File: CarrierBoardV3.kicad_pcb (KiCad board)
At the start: 4 copper layers, 92 x 96 mm, 102 parts, among them J1 USB_B_Micro, J10 Conn_02x26_Odd_Even, J11 SW1-12V_SHUNT, J12 SW9-3V3_SHUNT, J13 SW5-5V_SHUNT, J2 Conn_02x09_Odd_Even, J3 Barrel_Jack, J4 TX2iConnctor, J5 Conn_01x03_Male, J6 Conn_02x04_Odd_Even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

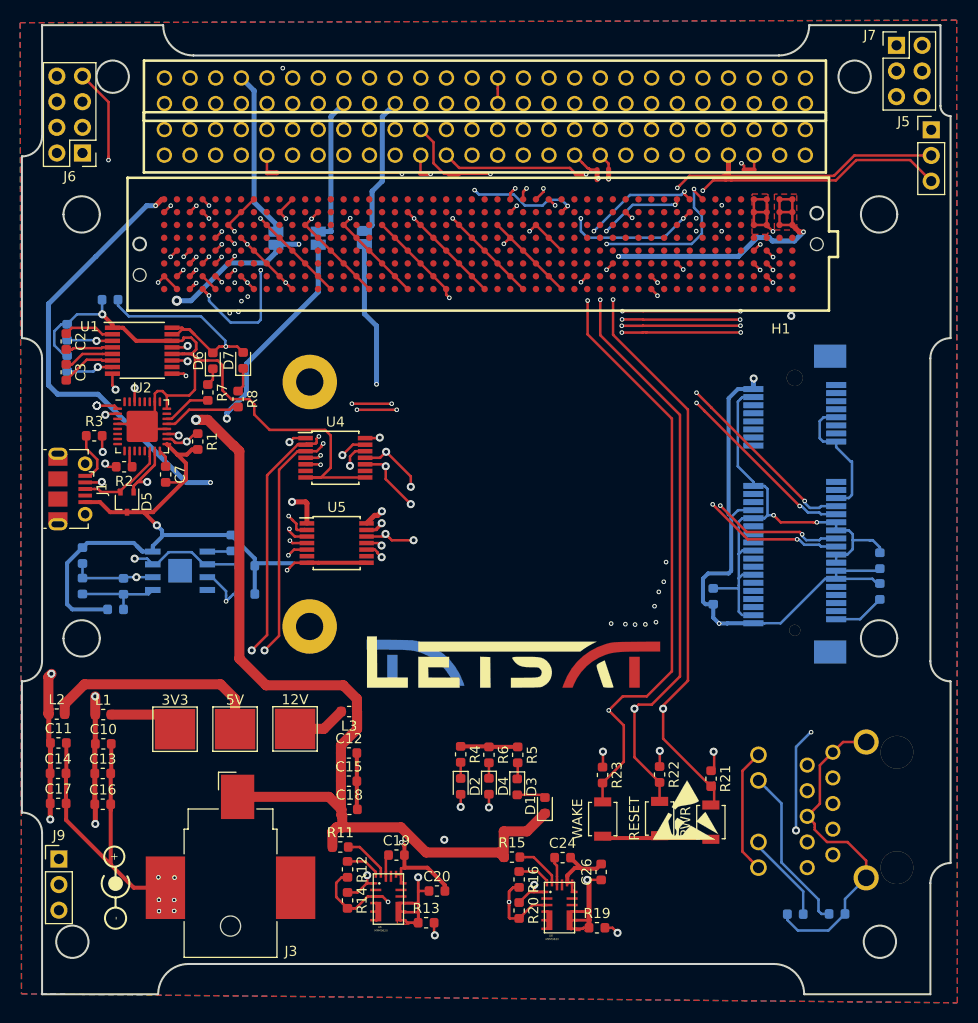
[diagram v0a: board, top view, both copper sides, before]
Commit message: traces complete, need help length matching becasue I can not seem to get it, no idea why???
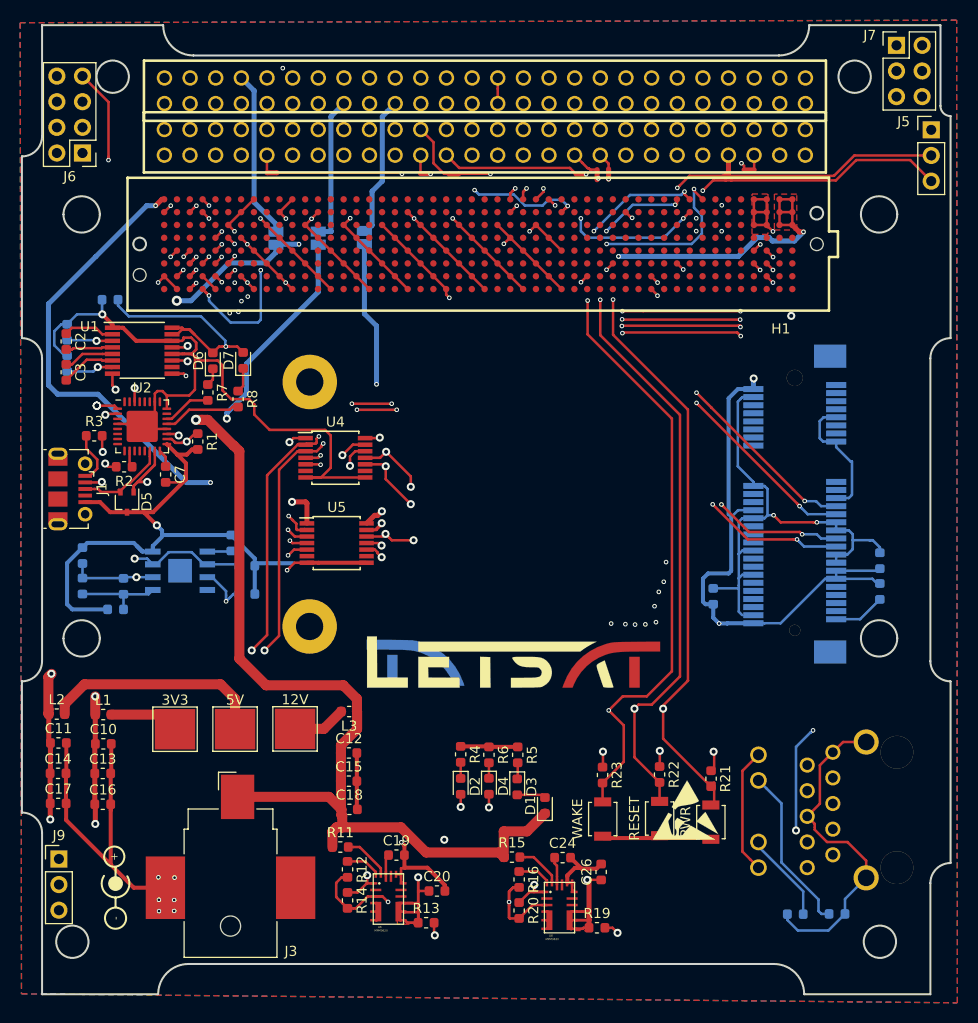
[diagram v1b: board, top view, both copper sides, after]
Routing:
- net SATA_RX+: track 71.6 -> 83.4 mm
- net SPI0_MI: track 81.6 -> 92.9 mm
- net SATA_RX-: track 73.0 -> 80.2 mm
- net SPI0_MISO: track 120.8 -> 127.7 mm
- net SPI0_CLK: track 117.0 -> 122.8 mm
- net I2C_DAT: track 59.1 -> 63.3 mm
- net SPI0_CS0#: track 135.2 -> 138.9 mm
- net I2C_GP1_DAT: track 86.4 -> 89.1 mm
- net SPI0_MO: track 79.4 -> 80.7 mm
- net SATA_TX+: track 81.7 -> 80.6 mm
- net SATA_TX-: track 83.5 -> 84.5 mm
- net UART0_TX: track 123.1 -> 124.0 mm
- net GBE_MDI3+: track 123.3 -> 123.9 mm

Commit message: Finished Rev 3 with correct orientation of TX2i connector
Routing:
- net SPI0_MO: track 80.7 -> 102.6 mm
- net GBE_MDI3+: track 123.9 -> 144.2 mm
- net GBE_MDI3-: track 107.9 -> 128.2 mm
- net GBE_MDI2-: track 101.6 -> 121.1 mm
- net GBE_MDI1-: track 102.8 -> 122.1 mm
- net GBE_MDI0+: track 98.1 -> 117.0 mm
- net GBE_MDI2+: track 116.4 -> 129.0 mm
- net SPI0_CK: track 81.9 -> 92.6 mm
- net GBE_MDI0-: track 98.5 -> 108.6 mm
- net SPI0_CS: track 87.9 -> 94.6 mm
- net GBE_MDI1+: track 103.1 -> 106.0 mm
- net SATA_RX-: track 80.2 -> 80.9 mm
- net SATA_RX+: track 83.4 -> 84.0 mm
